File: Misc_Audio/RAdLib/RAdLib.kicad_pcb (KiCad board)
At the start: 2 copper layers, 65 x 56.5 mm, 5 parts, among them J1 PinHeader_2x20_P2.54mm_Vertic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

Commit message: Checkpoint ... board is close to being done.  Still need to tweak the ground plane.
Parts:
- added C1: .1uF, Capacitor_THT:C_Disc_D5.0mm_W2.5mm_P2.50mm, F.Cu at (170.6, 135.9)
- added C101: .1uF, Capacitor_THT:C_Disc_D5.0mm_W2.5mm_P2.50mm, F.Cu at (148.0, 125.8)
- added C102: 4700pF, Capacitor_THT:C_Disc_D5.0mm_W2.5mm_P2.50mm, F.Cu at (157.0, 134.5)
- added C2: .1uF, Capacitor_THT:C_Disc_D5.0mm_W2.5mm_P2.50mm, F.Cu at (139.0, 139.5)
- added C201: .1uF, Capacitor_THT:C_Disc_D5.0mm_W2.5mm_P2.50mm, F.Cu at (175.7, 98.1)
- added C202: .1uF, Capacitor_THT:C_Disc_D5.0mm_W2.5mm_P2.50mm, F.Cu at (175.7, 108.5)
- added C203: .1uF, Capacitor_THT:C_Disc_D5.0mm_W2.5mm_P2.50mm, F.Cu at (150.5, 108.7)
- added C204: .1uF, Capacitor_THT:C_Disc_D5.0mm_W2.5mm_P2.50mm, F.Cu at (153.5, 101.6)
- added C3: .1uF, Capacitor_THT:C_Disc_D5.0mm_W2.5mm_P2.50mm, F.Cu at (120.9, 128.1)
- added C4: .1uF, Capacitor_THT:C_Disc_D5.0mm_W2.5mm_P2.50mm, F.Cu at (121.2, 107.4)
- added C5: 10uF, Capacitor_THT:CP_Radial_D5.0mm_P2.50mm, F.Cu at (126.0, 107.4)
- added C51: 10uF, Capacitor_THT:CP_Radial_D5.0mm_P2.50mm, F.Cu at (129.0, 140.4)
- added C52: 4700pF, Capacitor_THT:C_Disc_D5.0mm_W2.5mm_P2.50mm, F.Cu at (122.5, 115.9)
- added C53: 4700pF, Capacitor_THT:C_Disc_D5.0mm_W2.5mm_P2.50mm, F.Cu at (120.8, 122.2)
- added C54: 4700pF, Capacitor_THT:C_Disc_D5.0mm_W2.5mm_P2.50mm, F.Cu at (120.9, 134.1)
- added C55: 4700pF, Capacitor_THT:C_Disc_D5.0mm_W2.5mm_P2.50mm, F.Cu at (114.0, 135.8)
- added C56: 10uF, Capacitor_THT:CP_Radial_D5.0mm_P2.50mm, F.Cu at (112.5, 140.3)
- added C57: 4.7uF, Capacitor_THT:CP_Radial_D5.0mm_P2.50mm, F.Cu at (108.9, 134.2)
- added C58: 1000pF, Capacitor_THT:C_Disc_D5.0mm_W2.5mm_P2.50mm, F.Cu at (102.5, 127.1)
- added C59: 270pF, Capacitor_THT:C_Disc_D5.0mm_W2.5mm_P2.50mm, F.Cu at (110.1, 121.3)
- added C6: 10uF, Capacitor_THT:CP_Radial_D5.0mm_P2.50mm, F.Cu at (170.6, 139.3)
- added C60: .1uF, Capacitor_THT:C_Disc_D5.0mm_W2.5mm_P2.50mm, F.Cu at (110.1, 115.2)
- added C61: 10uF, Capacitor_THT:CP_Radial_D5.0mm_P2.50mm, F.Cu at (122.7, 99.7)
- added C62: .047uF, Capacitor_THT:C_Disc_D5.0mm_W2.5mm_P2.50mm, F.Cu at (118.4, 98.6)
- added C63: 220uF, Capacitor_THT:CP_Axial_L18.0mm_D8.0mm_P25.00mm_Horizontal, F.Cu at (103.7, 116.9)
- added C7: 10uF, Capacitor_THT:CP_Radial_D5.0mm_P2.50mm, F.Cu at (134.6, 115.9)
- added D1: 1N4148, Diode_THT:D_DO-35_SOD27_P7.62mm_Horizontal, F.Cu at (99.4, 141.2)
- added G***: LOGO, jrt-Graphics:AdLib_Logo, F.Cu at (141.8, 116.0)
- added J2: UART_Header, Connector_PinHeader_2.54mm:PinHeader_1x03_P2.54mm_Vertical, F.Cu at (137.8, 91.4)
- added J3: Power_Output_Header, Connector_PinHeader_2.54mm:PinHeader_1x03_P2.54mm_Vertical, F.Cu at (121.1, 91.4)
- added J4: I2C_Header, Connector_PinHeader_2.54mm:PinHeader_1x02_P2.54mm_Vertical, F.Cu at (128.3, 91.4)
- added J5: AudioJack3, jrt-Connectors:Jack_3.5mm_STX-3120-3B, F.Cu at (84.2, 101.8)
- added JP1: Jumper_2_Open, Connector_PinHeader_2.54mm:PinHeader_1x02_P2.54mm_Vertical, F.Cu at (137.4, 99.4)
- added Q1: 2N3904, Package_TO_SOT_THT:TO-92_HandSolder, F.Cu at (101.3, 135.2)
- added R1: 2.2K, Resistor_THT:R_Axial_DIN0204_L3.6mm_D1.6mm_P5.08mm_Horizontal, F.Cu at (156.6, 120.1)
- added R10: 2.2K, Resistor_THT:R_Axial_DIN0204_L3.6mm_D1.6mm_P5.08mm_Horizontal, F.Cu at (102.0, 141.2)
- added R101: 470R, Resistor_THT:R_Axial_DIN0204_L3.6mm_D1.6mm_P5.08mm_Horizontal, F.Cu at (149.0, 134.5)
- added R102: 470R, Resistor_THT:R_Axial_DIN0204_L3.6mm_D1.6mm_P5.08mm_Horizontal, F.Cu at (167.5, 134.5)
- added R11: 10K, Resistor_THT:R_Axial_DIN0204_L3.6mm_D1.6mm_P5.08mm_Horizontal, F.Cu at (110.6, 129.7)
- added R12: 2.2K, Resistor_THT:R_Axial_DIN0204_L3.6mm_D1.6mm_P5.08mm_Horizontal, F.Cu at (105.5, 127.1)
- added R13: 8.2K, Resistor_THT:R_Axial_DIN0204_L3.6mm_D1.6mm_P5.08mm_Horizontal, F.Cu at (110.6, 124.5)
- added R14: 10R, Resistor_THT:R_Axial_DIN0204_L3.6mm_D1.6mm_P5.08mm_Horizontal, F.Cu at (112.4, 98.6)
- added R15: 10K, Resistor_THT:R_Axial_DIN0204_L3.6mm_D1.6mm_P5.08mm_Horizontal, F.Cu at (109.7, 93.5)
- added R16: 10R, Resistor_THT:R_Axial_DIN0204_L3.6mm_D1.6mm_P5.08mm_Horizontal, F.Cu at (89.5, 106.8)
- added R17: 10R, Resistor_THT:R_Axial_DIN0204_L3.6mm_D1.6mm_P5.08mm_Horizontal, F.Cu at (89.5, 96.8)
- added R2: 2.2K, Resistor_THT:R_Axial_DIN0204_L3.6mm_D1.6mm_P5.08mm_Horizontal, F.Cu at (130.4, 113.3)
- added R201: 4.7K, Resistor_THT:R_Axial_DIN0204_L3.6mm_D1.6mm_P5.08mm_Horizontal, F.Cu at (171.2, 96.8)
- added R202: 4.7K, Resistor_THT:R_Axial_DIN0204_L3.6mm_D1.6mm_P5.08mm_Horizontal, F.Cu at (168.9, 101.8)
- added R203: 2.2K, Resistor_THT:R_Axial_DIN0204_L3.6mm_D1.6mm_P5.08mm_Horizontal, F.Cu at (166.5, 101.8)
- added R204: 3.3K, Resistor_THT:R_Axial_DIN0204_L3.6mm_D1.6mm_P5.08mm_Horizontal, F.Cu at (164.1, 96.7)
- added R205: 1K, Resistor_THT:R_Axial_DIN0204_L3.6mm_D1.6mm_P5.08mm_Horizontal, F.Cu at (138.2, 103.6)
- added R3: 2.2K, Resistor_THT:R_Axial_DIN0204_L3.6mm_D1.6mm_P5.08mm_Horizontal, F.Cu at (125.3, 115.9)
- added R4: 12K, Resistor_THT:R_Axial_DIN0204_L3.6mm_D1.6mm_P5.08mm_Horizontal, F.Cu at (116.1, 123.2)
- added R5: 10K, Resistor_THT:R_Axial_DIN0204_L3.6mm_D1.6mm_P5.08mm_Horizontal, F.Cu at (113.6, 123.2)
- added R6: 2.2K, Resistor_THT:R_Axial_DIN0204_L3.6mm_D1.6mm_P5.08mm_Horizontal, F.Cu at (116.1, 130.5)
- added R7: 2.2K, Resistor_THT:R_Axial_DIN0204_L3.6mm_D1.6mm_P5.08mm_Horizontal, F.Cu at (113.6, 125.4)
- added R8: 12K, Resistor_THT:R_Axial_DIN0204_L3.6mm_D1.6mm_P5.08mm_Horizontal, F.Cu at (116.7, 136.9)
- added R9: 10K, Resistor_THT:R_Axial_DIN0204_L3.6mm_D1.6mm_P5.08mm_Horizontal, F.Cu at (116.7, 139.3)
- added REF**: OSHW-Logo_5.7x6mm_SilkScreen, Symbol:OSHW-Logo_5.7x6mm_SilkScreen, F.Cu at (91.9, 113.3)
- added REF**: MountingHole_2.7mm_M2.5_DIN965, MountingHole:MountingHole_2.7mm_M2.5_DIN965, F.Cu at (79.4, 140.7)
- added REF**: MountingHole_2.7mm_M2.5_DIN965, MountingHole:MountingHole_2.7mm_M2.5_DIN965, F.Cu at (79.4, 91.2)
- added RV1: 10K, jrt-Potentiometers:Potentiometer_Bourns_91A1x_A24, F.Cu at (96.2, 126.3)
- added RV1: 10K, jrt-Potentiometers:Potentiometer_Bourns_91A1x_A24, F.Cu at (91.8, 126.3)
- added RV1: 10K, jrt-Potentiometers:Potentiometer_Bourns_91A1x_A24, F.Cu at (87.3, 126.3)
- added U1: YM3812, Package_DIP:DIP-24_W15.24mm_Socket, F.Cu at (174.2, 135.9)
- added U101: 74AHCT04, Package_DIP:DIP-14_W7.62mm_Socket, F.Cu at (151.5, 130.8)
- added U2: YM3014B, Package_DIP:DIP-8_W7.62mm_Socket, F.Cu at (143.1, 135.8)
- added U201: 74LVC245A, Package_DIP:DIP-20_W7.62mm, F.Cu at (179.2, 103.2)
- added U202: 74HCT245, Package_DIP:DIP-20_W7.62mm, F.Cu at (179.2, 113.7)
- added U203: 74AHCT125, Package_DIP:DIP-14_W7.62mm, F.Cu at (153.9, 113.8)
- added U204: M24C01-FDW, Package_DIP:DIP-8_W7.62mm_Socket, F.Cu at (150.1, 96.5)
- added U3: RC4136, Package_DIP:DIP-14_W7.62mm, F.Cu at (131.7, 135.7)
- added U4: LM386, Package_DIP:DIP-8_W7.62mm, F.Cu at (110.5, 102.3)
- added Y101: 3.58MHz Crystal, Crystal:Crystal_HC49-4H_Vertical, F.Cu at (156.0, 139.5)
- J1: value PinHeader_2x20_P2.54mm_Vertical -> Raspberry_Pi_2_3
- moved J1 54.7 mm to (148.6, 92.5)
- moved REF** 54.7 mm to (201.7, 91.2)
- moved REF** 54.7 mm to (143.7, 91.2)
- moved REF** 54.7 mm to (143.7, 140.7)
- moved REF** 54.7 mm to (201.7, 140.7)
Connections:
- J1 pad 1: (no net) -> +3V3
- J1 pad 10: (no net) -> UART_RXD
- J1 pad 11: (no net) -> Net-(J1-Pad11)
- J1 pad 12: (no net) -> Net-(J1-Pad12)
- J1 pad 13: (no net) -> A0
- J1 pad 14: (no net) -> GND
- J1 pad 15: (no net) -> IRQ
- J1 pad 16: (no net) -> Net-(J1-Pad16)
- J1 pad 17: (no net) -> Net-(J1-Pad17)
- J1 pad 18: (no net) -> Net-(J1-Pad18)
- J1 pad 19: (no net) -> Net-(J1-Pad19)
- J1 pad 2: (no net) -> +5V
- J1 pad 20: (no net) -> GND
- J1 pad 21: (no net) -> Net-(J1-Pad21)
- J1 pad 22: (no net) -> ~RST
- J1 pad 23: (no net) -> Net-(J1-Pad23)
- J1 pad 24: (no net) -> ~CS
- J1 pad 25: (no net) -> GND
- J1 pad 26: (no net) -> READ
- J1 pad 27: (no net) -> ID_SDA
- J1 pad 28: (no net) -> ID_SCL
- J1 pad 29: (no net) -> Net-(J1-Pad29)
- J1 pad 3: (no net) -> I2C_SDA
- J1 pad 30: (no net) -> GND
- J1 pad 31: (no net) -> D7
- J1 pad 32: (no net) -> D6
- J1 pad 33: (no net) -> D5
- J1 pad 34: (no net) -> GND
- J1 pad 35: (no net) -> D4
- J1 pad 36: (no net) -> D3
- J1 pad 37: (no net) -> D2
- J1 pad 38: (no net) -> D0
- J1 pad 39: (no net) -> GND
- J1 pad 4: (no net) -> +5V
- J1 pad 40: (no net) -> D1
- J1 pad 5: (no net) -> I2C_SCL
- J1 pad 6: (no net) -> GND
- J1 pad 7: (no net) -> Net-(J1-Pad7)
- J1 pad 8: (no net) -> UART_TXD
- J1 pad 9: (no net) -> GND
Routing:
- net +5V: track 0.00 -> 223.7 mm, vias 0 -> 4
- net +3V3: track 0.00 -> 101.6 mm, vias 0 -> 2
- net ~OPL_RD: track 0.00 -> 76.0 mm, vias 0 -> 3
- net ~OPL_WR: track 0.00 -> 70.0 mm, vias 0 -> 1
- net /DAC_SYNC: track 0.00 -> 60.3 mm, vias 0 -> 3
- net ID_SCL: track 0.00 -> 51.3 mm, vias 0 -> 3
- net ID_SDA: track 0.00 -> 51.1 mm, vias 0 -> 2
- net ~OPL_CS: track 0.00 -> 50.4 mm, vias 0 -> 2
- net ~OPL_RST: track 0.00 -> 45.7 mm, vias 0 -> 2
- net /DAC_CLK: track 0.00 -> 45.3 mm, vias 0 -> 2
- net /DAC_DATA: track 0.00 -> 45.0 mm, vias 0 -> 1
- net OPL_A0: track 0.00 -> 44.9 mm, vias 0 -> 4
- net READ: track 0.00 -> 39.5 mm, vias 0 -> 1
- net I2C_SCL: track 0.00 -> 37.3 mm
- net OPL_D0: track 0.00 -> 34.6 mm
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- added copper zone on B.Cu, net GND
- added copper zone on F.Cu, net GND
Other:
- board size 65 x 56.5 mm -> 129.2 x 56.5 mm
- net class VCC added: clearance 0.2, trace_width 0.35, via_dia 0.8, via_drill 0.4
- board text added: "3V3"
- board text added: "5V"
- board text added: "GND"
- board text added: "OPL2 FM Synthesizer for Raspberry Pi Copyright 2019 Jason R. Thorpe."
- board text added: "RAdLib"
- board text added: "RXD"
- board text added: "Rev 1.0"
- board text added: "SCL"
- board text added: "SDA"
- board text added: "TXD"
- board text added: "Write Enable"

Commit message: Close to final?
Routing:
- net GND: track 4.48 -> 336.4 mm, vias 0 -> 6
- net +5V: track 223.7 -> 239.0 mm, vias 4 -> 5
- net READ: track 39.5 -> 42.8 mm
- removed copper zone on B.Cu, net GND
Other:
- net class GND added: clearance 0.2, trace_width 0.35, via_dia 0.8, via_drill 0.4

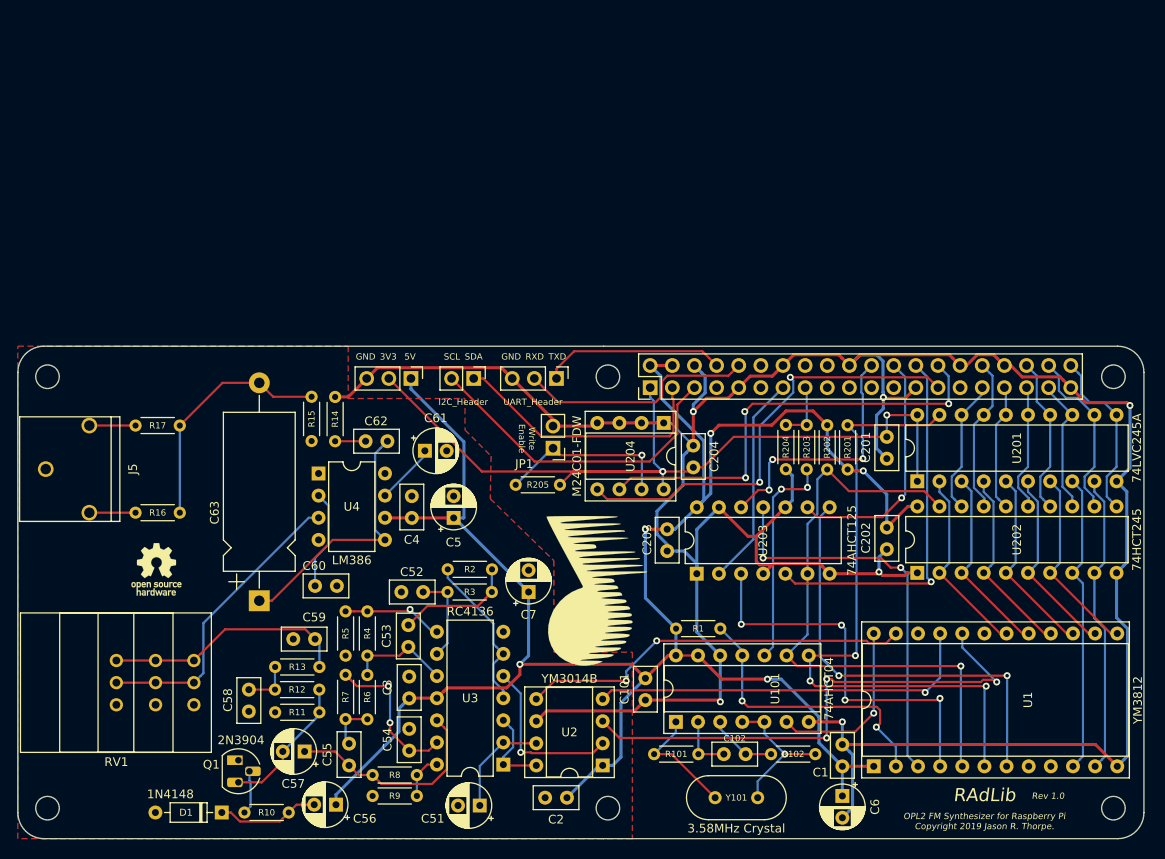
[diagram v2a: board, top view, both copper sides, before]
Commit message: Rework the clock to use a self-contained oscillator package.  Remove dependencies on the 7404 in the bus interface.
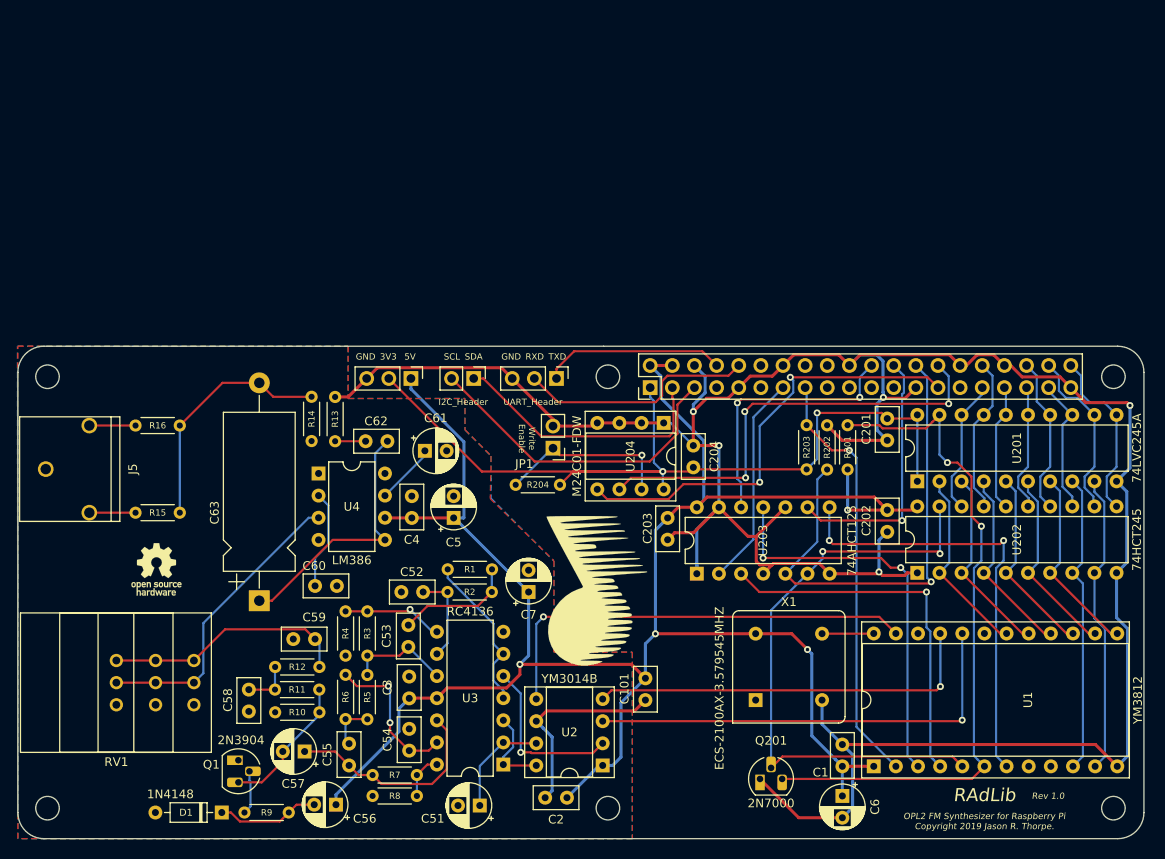
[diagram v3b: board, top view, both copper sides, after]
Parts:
- removed C102: 4700pF, Capacitor_THT:C_Disc_D5.0mm_W2.5mm_P2.50mm
- removed the R1 at (156.6, 120.1)
- removed R101, R102: 470R, Resistor_THT:R_Axial_DIN0204_L3.6mm_D1.6mm_P5.08mm_Horizontal
- removed the R204 at (164.1, 96.7)
- removed U101: 74AHCT04, Package_DIP:DIP-14_W7.62mm_Socket
- removed Y101: 3.58MHz Crystal, Crystal:Crystal_HC49-4H_Vertical
- added Q201: 2N7000, Package_TO_SOT_THT:TO-92_HandSolder, F.Cu at (161.2, 137.3)
- added X1: ECS-2100AX-3.579545MHZ, Oscillator:Oscillator_DIP-8, F.Cu at (160.7, 128.3)
- R202: value 4.7K -> 3.3K
- R203: value 2.2K -> 3.3K
- R204: renamed from R205; value 1K -> 3.3K
- moved R203 5.07 mm to (166.5, 96.8), turned to 270 degrees
- moved C201 2.10 mm to (175.8, 96.0)
- moved C202 2.00 mm to (175.8, 106.5)
- moved C203 1.30 mm to (150.6, 107.4)
- renumbered R2 to R1, R11 to R10, R12 to R11, R13 to R12, R14 to R13, R15 to R14, R16 to R15, R17 to R16, R3 to R2, R4 to R3, R5 to R4, R6 to R5, R7 to R6, R8 to R7, R9 to R8, R10 to R9
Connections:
- J1 pad 15: IRQ -> ~OPL_IRQ
- R202 pad 1: ~OPL_WR -> READ
- R202 pad 2: +5V -> GND
- R203 pad 1: Net-(R203-Pad1) -> ~OPL_IRQ
- R203 pad 2: IRQ -> +3V3
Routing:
- net Net-(R203-Pad1): track 25.1 -> 0.00 mm, vias 2 -> 0
- net Net-(R102-Pad1): track 17.0 -> 0.00 mm, vias 1 -> 0
- net ~OPL_IRQ: track 33.2 -> 49.2 mm, vias 2 -> 1
- net OPL_CLK: track 20.5 -> 5.94 mm, vias 1 -> 0
- net READ: track 42.8 -> 56.8 mm
- net Net-(R101-Pad1): track 13.8 -> 0.00 mm
- net /DAC_SYNC: track 60.3 -> 51.2 mm, vias 3 -> 1
- net Net-(C102-Pad2): track 7.83 -> 0.00 mm
- net IRQ: track 6.74 -> 0.00 mm
- net Net-(C102-Pad1): track 6.64 -> 0.00 mm
- net /DAC_CLK: track 45.3 -> 51.0 mm, vias 2 -> 1
- net +5V: track 239.0 -> 233.8 mm, vias 5 -> 4
- net ~OPL_RD: track 76.0 -> 79.0 mm, vias 3 -> 2
- net +3V3: track 101.6 -> 104.0 mm
- net OPL_A0: track 44.9 -> 42.8 mm, vias 4 -> 1
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- added copper zone on B.Cu, net GND

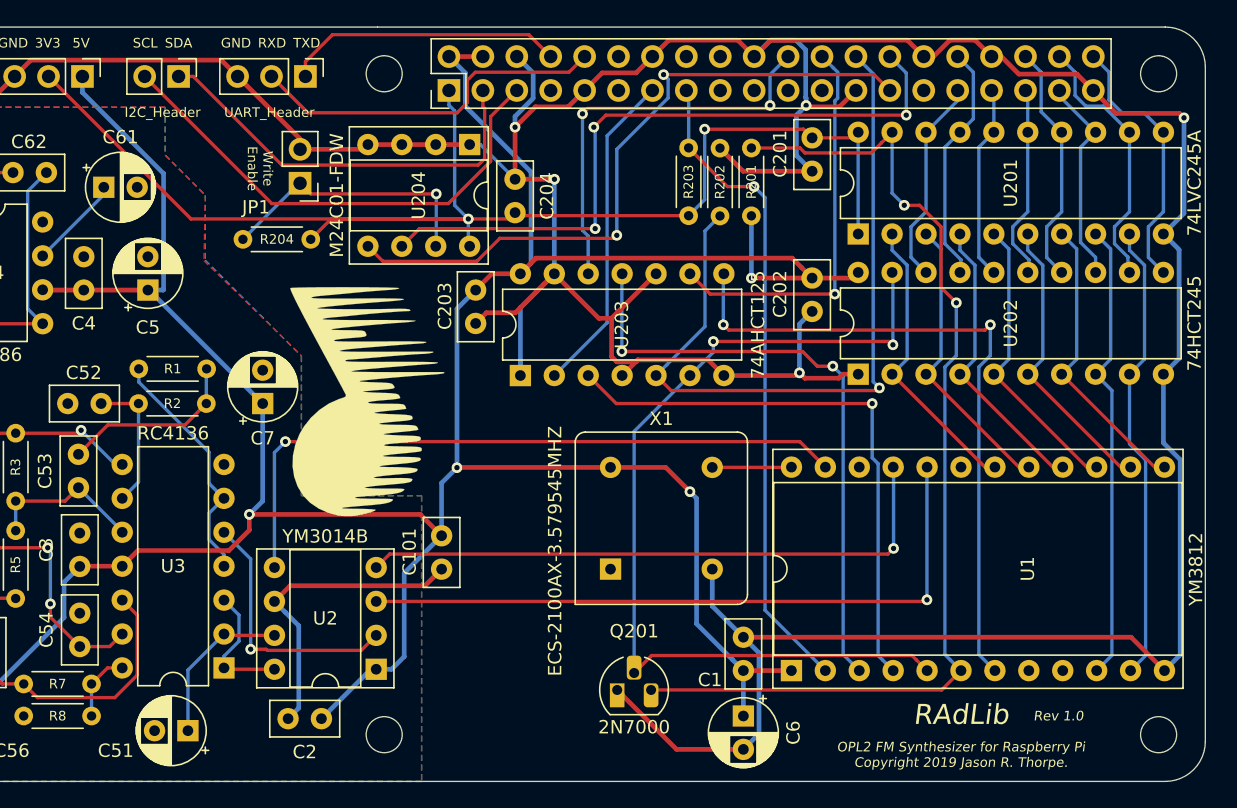
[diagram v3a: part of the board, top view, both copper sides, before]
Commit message: Initial rework to simplify the bus interface (removing U202 and U203).
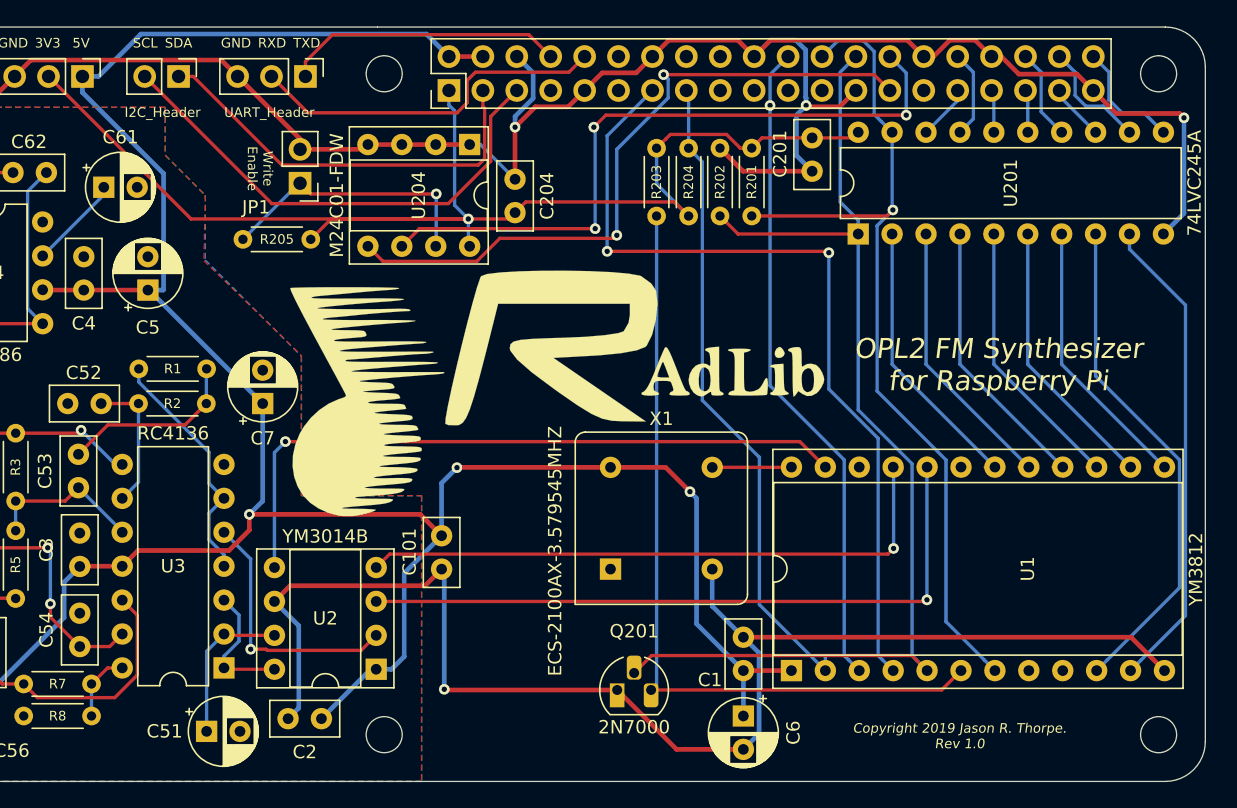
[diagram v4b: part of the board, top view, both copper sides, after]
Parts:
- removed C202, C203: .1uF, Capacitor_THT:C_Disc_D5.0mm_W2.5mm_P2.50mm
- removed the R204 at (138.2, 103.6)
- removed U202: 74HCT245, Package_DIP:DIP-20_W7.62mm
- removed U203: 74AHCT125, Package_DIP:DIP-14_W7.62mm
- added G***: LOGO, jrt-Graphics:AdLib_Logo_Text, F.Cu at (169.8, 113.1)
- added G***: LOGO, jrt-Graphics:Volvo_R_small, F.Cu at (156.1, 111.6)
- added R203: 3.3K, Resistor_THT:R_Axial_DIN0204_L3.6mm_D1.6mm_P5.08mm_Horizontal, F.Cu at (164.1, 96.8)
- added R205: 3.3K, Resistor_THT:R_Axial_DIN0204_L3.6mm_D1.6mm_P5.08mm_Horizontal, F.Cu at (138.2, 103.6)
- R201: value 4.7K -> 3.3K
- moved R201 5.09 mm to (171.2, 101.8), turned to 90 degrees
- moved C51 1.40 mm to (130.4, 140.4), turned to 0 degrees
- renumbered R203 to R204
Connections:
- J1 pad 13: A0 -> OPL_A0
- J1 pad 22: ~RST -> ~OPL_RST
- J1 pad 24: ~CS -> ~OPL_CS
- J1 pad 26: READ -> ~OPL_WR
- R201 pad 1: ~OPL_RD -> ~OPL_CS
- R201 pad 2: +5V -> +3V3
- R202 pad 1: READ -> ~OPL_WR
- U201 pad 1: +3V3 -> ~OPL_WR
- U201 pad 19: ~OPL_RD -> ~OPL_CS
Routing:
- net GND: track 334.3 -> 255.0 mm, vias 5 -> 4
- net READ: track 56.8 -> 0.00 mm, vias 1 -> 0
- net +5V: track 233.8 -> 190.3 mm, vias 4 -> 3
- net ~RST: track 30.7 -> 0.00 mm, vias 2 -> 0
- net ~CS: track 29.8 -> 0.00 mm, vias 1 -> 0
- net A0: track 24.4 -> 0.00 mm
- net OPL_A0: track 42.8 -> 63.4 mm, vias 1 -> 2
- net ~OPL_RD: track 79.0 -> 59.5 mm, vias 2 -> 0
- net ~OPL_CS: track 51.0 -> 66.7 mm, vias 2 -> 1
- net ~OPL_WR: track 69.5 -> 83.3 mm, vias 2 -> 0
- net D4: track 14.7 -> 3.20 mm
- net D6: track 18.1 -> 6.57 mm
- net D5: track 14.6 -> 3.20 mm
- net D7: track 15.5 -> 4.11 mm
- net D3: track 18.2 -> 6.79 mm
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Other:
- board text added: "Copyright 2019 Jason R. Thorpe. Rev 1.0"
- board text added: "OPL2 FM Synthesizer for Raspberry Pi"
- board text removed: "OPL2 FM Synthesizer for Raspberry Pi Copyright 2019 Jason R. Thorpe."
- board text removed: "RAdLib"
- board text removed: "Rev 1.0"

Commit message: Additional tweaks, silly graphics.
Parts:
- removed C101: .1uF, Capacitor_THT:C_Disc_D5.0mm_W2.5mm_P2.50mm
- U204: value M24C01-FDW -> 24Cxx
- moved C204 24.6 mm to (174.4, 114.6)
- moved JP1 23.4 mm to (158.3, 109.9)
- moved R205 23.4 mm to (159.1, 114.1)
- moved U204 23.4 mm to (171.0, 107.0)
- moved G*** 21.7 mm to (152.6, 99.8)
- moved G*** 20.9 mm to (137.4, 102.3)
- moved C2 15.0 mm to (154.0, 139.7)
- moved U2 10.9 mm to (154.0, 136.1)
- moved G*** 2.48 mm to (143.5, 117.8)
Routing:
- net GND: track 255.0 -> 512.4 mm, vias 4 -> 9
- net /DAC_CLK: track 51.0 -> 36.7 mm
- net Net-(U2-Pad8): track 9.83 -> 21.0 mm
- net Net-(C51-Pad1): track 11.6 -> 22.8 mm
- net /DAC_SYNC: track 51.2 -> 40.3 mm
- net /DAC_DATA: track 45.4 -> 34.9 mm
- net ID_SDA: track 51.1 -> 42.2 mm
- net +3V3: track 101.7 -> 110.2 mm, vias 1 -> 2
- net I2C_SCL: track 37.3 -> 30.5 mm
- net Net-(U2-Pad2): track 19.5 -> 25.6 mm, vias 1 -> 0
- net OPL_A0: track 63.4 -> 57.3 mm
- net I2C_SDA: track 31.0 -> 25.7 mm
- net ID_SCL: track 51.3 -> 46.3 mm
- net Net-(JP1-Pad1): track 20.5 -> 18.8 mm, vias 1 -> 0
- net +5V: track 190.3 -> 189.2 mm, vias 3 -> 2
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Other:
- board text added: "Copyright 2019 Jason R. Thorpe."
- board text added: "ID ROM"
- board text added: "Rev 1.0"
- board text removed: "Copyright 2019 Jason R. Thorpe. Rev 1.0"
